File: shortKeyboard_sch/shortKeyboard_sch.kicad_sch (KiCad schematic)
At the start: 17 parts, among them J1 MPU5060 2.54 1x8, J10 In, J11 Conn_01x06, J12 Out, J2 TP4056 bat/out 2.54, J3 TP4056 in 2.54 1x6, J4 USB Power Data 2.54, J5 esp32 left 2.54 MALE, J6 esp32 right 2.54 MALE, J7 ESP32 USB 2.54 Data, J8 Li-Ion Batter 2.54, J9 Buttons Connector 2.54

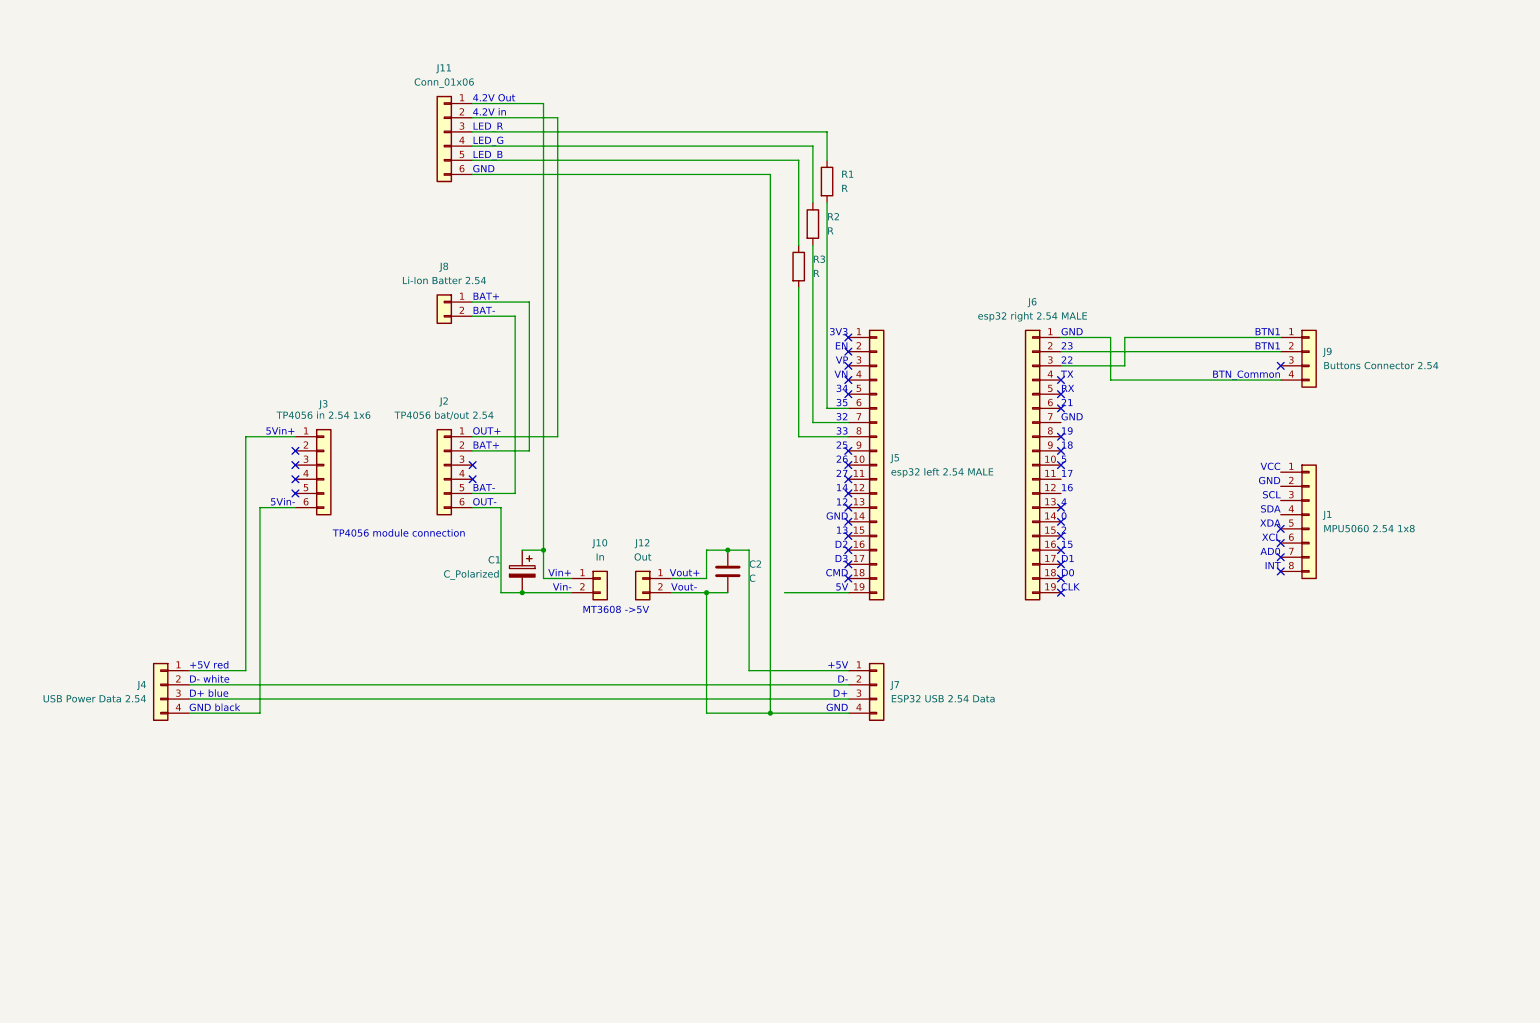
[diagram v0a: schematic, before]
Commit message: SCH change buttons connector to B1_GND_B2_GND - so buttons conectors independent
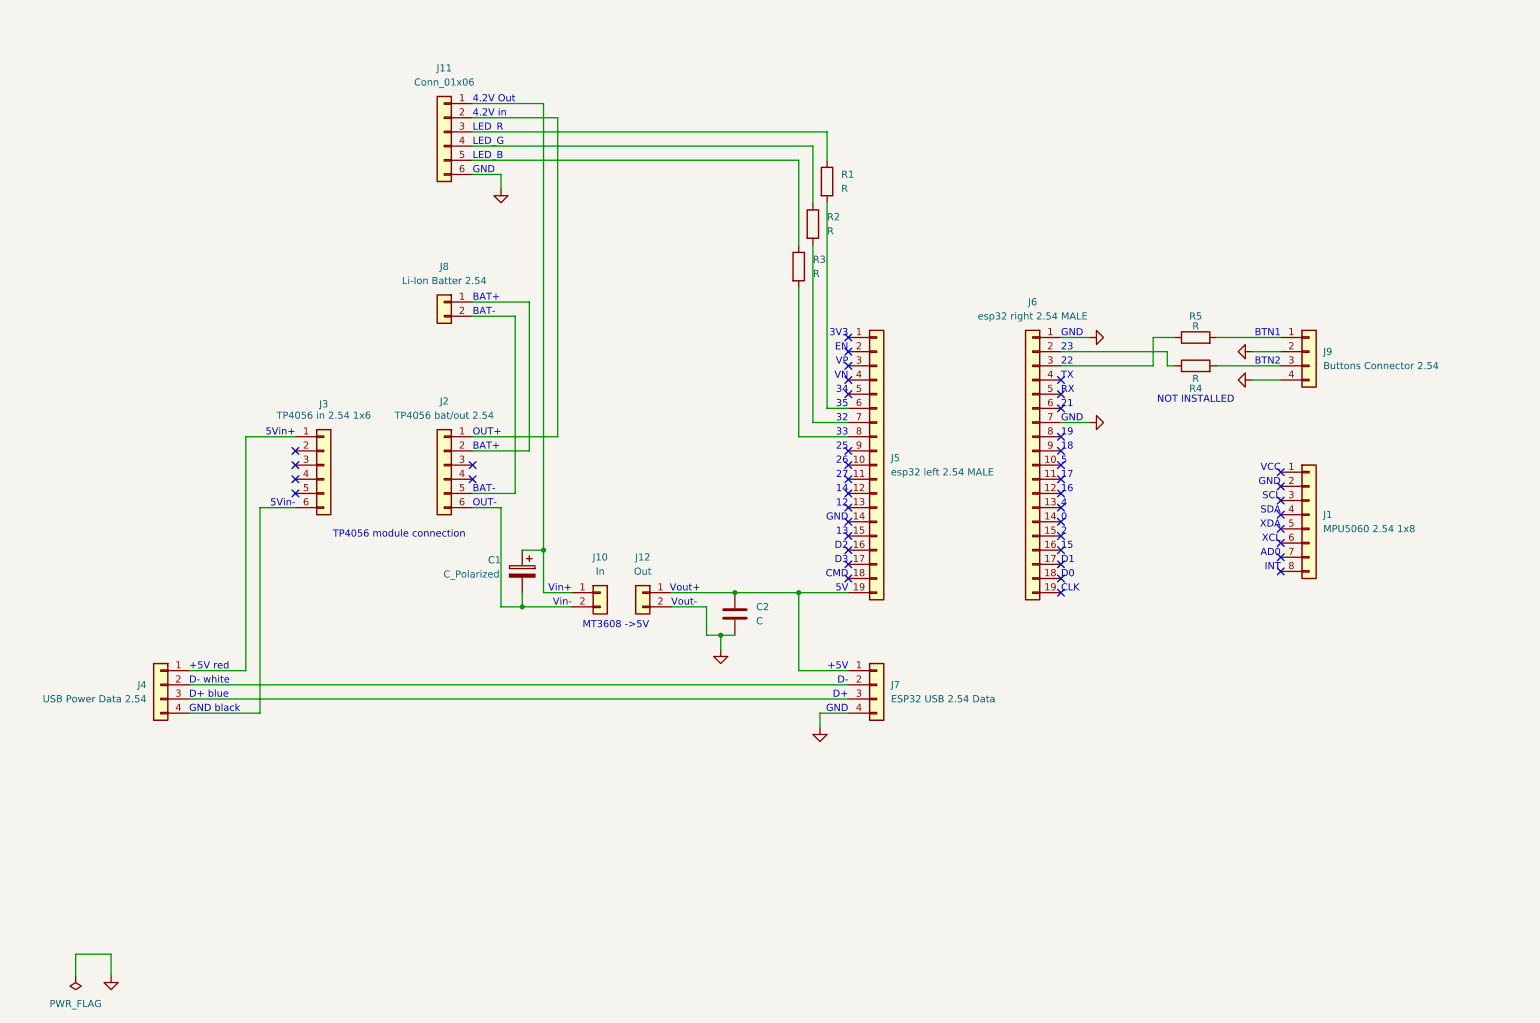
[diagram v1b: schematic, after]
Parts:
- added R4, R5: R, symbol Device:R
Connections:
- net GND: now reaches C2.2, J11.6 (Pin_6), J12.2 (Pin_2), J7.4 (Pin_4)
- net GND: now also J6.1 (Pin_1), J6.7 (Pin_7), J9.2 (Pin_2), J9.4 (Pin_4)
- net at C2.1, J12.1 (Pin_1), J7.1 (Pin_1): now also J5.19 (Pin_19)
- net at J6.2 (Pin_2): now also R4.1; no longer J9.2 (Pin_2)
- net at J6.3 (Pin_3): now also R5.1; no longer J9.1 (Pin_1)
- net at J9.3 (Pin_3): now also R4.2
- new net: J9.1 (Pin_1), R5.2
- no-connect marks 39 -> 44
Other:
- note added: "BTN2"
- note added: "NOT INSTALLED"
- note removed: "BTN_Common"
- moved on the sheet: C2, J10, J12

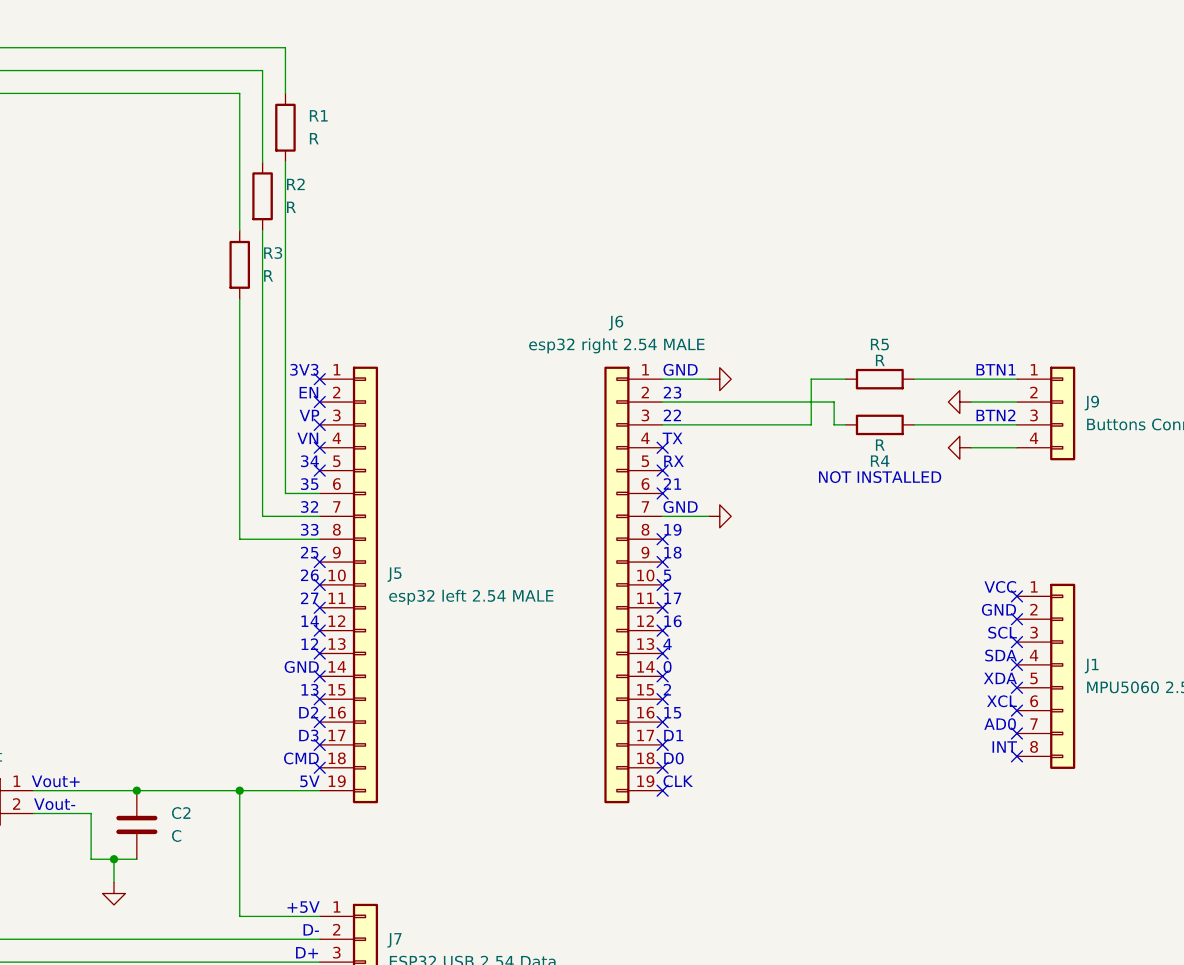
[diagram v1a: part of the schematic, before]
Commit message: update schematic, add mpu pins
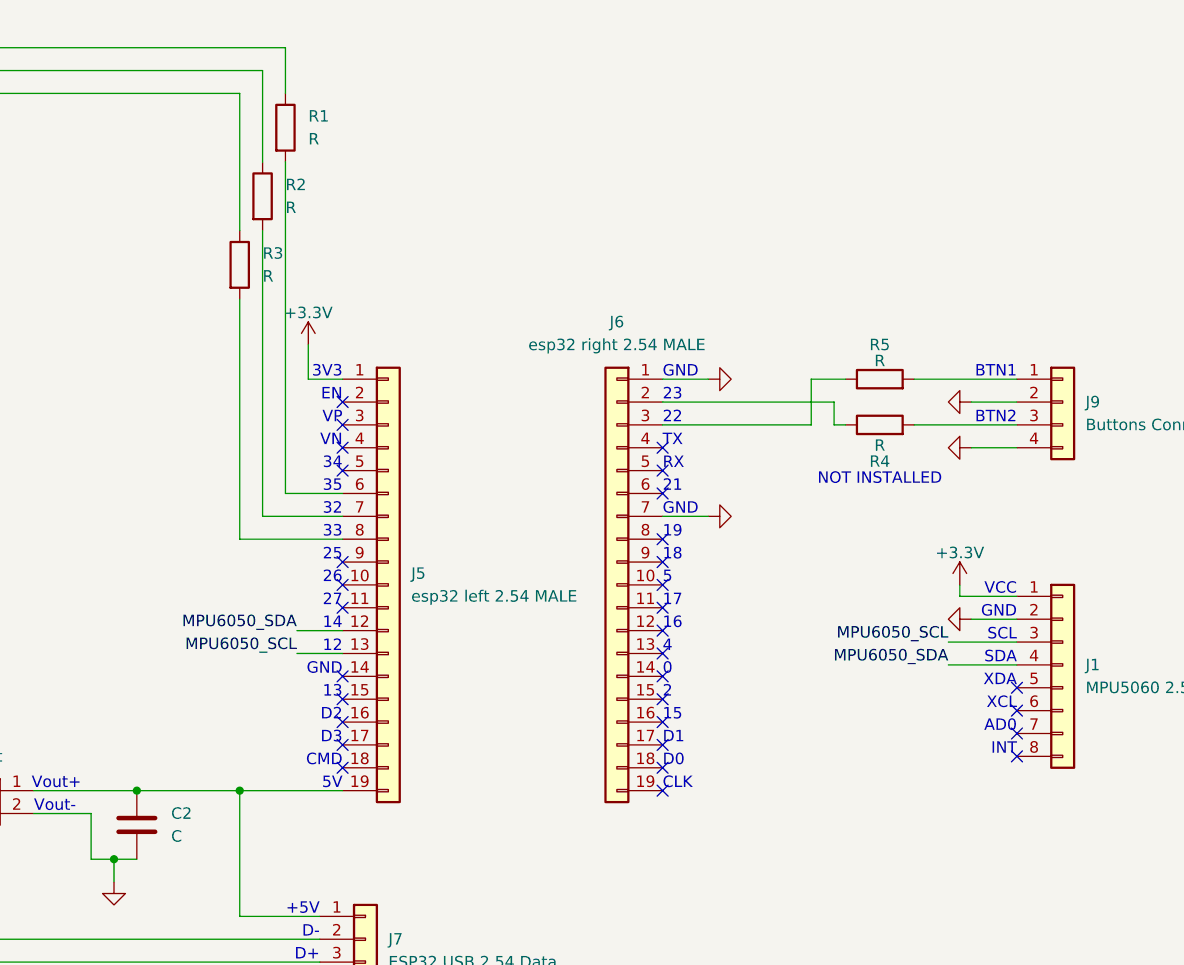
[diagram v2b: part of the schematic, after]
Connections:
- net GND: now also J1.2 (Pin_2)
- net +3.3V: now reaches J1.1 (Pin_1)
- net +3.3V: now also J5.1 (Pin_1)
- net MPU6050_SCL: now reaches J1.3 (Pin_3)
- net MPU6050_SCL: now also J5.13 (Pin_13)
- net MPU6050_SDA: now reaches J1.4 (Pin_4)
- net MPU6050_SDA: now also J5.12 (Pin_12)
- no-connect marks 44 -> 37
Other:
- moved on the sheet: J5

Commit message: intermediate new pcb version again
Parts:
- removed C1: C_Polarized, symbol Device:C_Polarized
- removed J1: MPU5060 2.54 1x8, symbol Connector_Generic:Conn_01x08
- removed J10: In, symbol Connector_Generic:Conn_01x02
- removed J11: Conn_01x06, symbol Connector_Generic:Conn_01x06
- removed J12: Out, symbol Connector_Generic:Conn_01x02
- removed J2: TP4056 bat/out 2.54, symbol Connector_Generic:Conn_01x06
- removed J3: TP4056 in 2.54 1x6, symbol Connector_Generic:Conn_01x06
- removed J4: USB Power Data 2.54, symbol Connector_Generic:Conn_01x04
- removed J5: esp32 left 2.54 MALE, symbol Connector_Generic:Conn_01x19
- removed J6: esp32 right 2.54 MALE, symbol Connector_Generic:Conn_01x19
- removed J7: ESP32 USB 2.54 Data, symbol Connector_Generic:Conn_01x04
- removed J8: Li-Ion Batter 2.54, symbol Connector_Generic:Conn_01x02
- removed J9: Buttons Connector 2.54, symbol Connector_Generic:Conn_01x04
- added C1: 22p, Capacitor_SMD:C_0805_2012Metric_Pad1.18x1.45mm_HandSolder, symbol Device:C
- added C3: 0.1u, Capacitor_SMD:C_0805_2012Metric_Pad1.18x1.45mm_HandSolder, symbol Device:C
- added C4, C5, C7: 0.1uF, Capacitor_SMD:C_0805_2012Metric_Pad1.18x1.45mm_HandSolder, symbol Device:C
- added C6: 10uF 16V, Capacitor_Tantalum_SMD:CP_EIA-3216-18_Kemet-A_HandSolder, symbol Device:C_Polarized
- added C8: 22uF 6.3V, Capacitor_Tantalum_SMD:CP_EIA-3216-18_Kemet-A_HandSolder, symbol Device:C_Polarized
- added D1, D2, D3, D5, D6: LED, LED_SMD:LED_0805_2012Metric_Pad1.15x1.40mm_HandSolder, symbol Device:LED
- added D4: SS34, Diode_SMD:D_SMA, symbol Diode:SS34
- added J1: PH2.0-4, lw_kicadLib:PH2.0-4, symbol lw_kicadLib:PH2.0-4
- added J2, J3, J6: PH2.0-2, lw_kicadLib:PH2.0-2, symbol lw_kicadLib:PH2.0-2
- added J4: WF-8, lw_kicadLib:WF-8, symbol lw_kicadLib:WF-8
- added J5: PH2.0-5, lw_kicadLib:PH2.0-5, symbol lw_kicadLib:PH2.0-5
- added Q1, Q2: SS8050, Package_TO_SOT_SMD:SOT-23, symbol Transistor_BJT:SS8050
- added Q3: AO3401A, Package_TO_SOT_SMD:SOT-23, symbol Transistor_FET:AO3401A
- added R10, R11, R6: 10к (5%), Resistor_SMD:R_0805_2012Metric_Pad1.20x1.40mm_HandSolder, symbol Device:R
- added R12, R13: 1k, Resistor_SMD:R_0805_2012Metric_Pad1.20x1.40mm_HandSolder, symbol Device:R
- added R14, R16, R18: 2.7k, Resistor_SMD:R_0805_2012Metric_Pad1.20x1.40mm_HandSolder, symbol Device:R
- added R15: 10k, Resistor_SMD:R_0805_2012Metric_Pad1.20x1.40mm_HandSolder, symbol Device:R
- added R17: 0, Resistor_SMD:R_0805_2012Metric_Pad1.20x1.40mm_HandSolder, symbol Device:R
- added U1: CH340G, Package_SO:SOIC-16_3.9x9.9mm_P1.27mm, symbol Interface_USB:CH340G
- added U2: (no value), lw_kicadLib:TP4056_Module_CD_MicroUsb, symbol lw_kicadLib:TP4056_Module
- added U3: AMS1117-3.3, Package_TO_SOT_SMD:SOT-223-3_TabPin2, symbol Regulator_Linear:AMS1117-3.3
- added U4: ESP32-WROVER, lw_kicadLib:ESP32-WROVER-handSoldering, symbol lw_kicadLib:ESP32-WROVER
- added Y1: 12M, Crystal:Crystal_SMD_HC49-SD_HandSoldering, symbol Device:Crystal
- C2: value C -> 22p; footprint (none) -> Capacitor_SMD:C_0805_2012Metric_Pad1.18x1.45mm_HandSolder
- R1, R4: value R -> ?k; footprint (none) -> Resistor_SMD:R_0805_2012Metric_Pad1.20x1.40mm_HandSolder
- R2, R3: value R -> 3.3k; footprint (none) -> Resistor_SMD:R_0805_2012Metric_Pad1.20x1.40mm_HandSolder
- R5: value R -> 10к (5%); footprint (none) -> Resistor_SMD:R_0805_2012Metric_Pad1.20x1.40mm_HandSolder
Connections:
- net GND: now also C1.2, C3.2, C4.2, C5.2, C6.2, C7.2, C8.2, J1.4 (Pin_1), J2.2 (Pin_2), J3.2 (Pin_2), J4.2 (Pin_2), J5.5 (Pin_1), R14.2, R15.2, R16.2, R18.2, U1.1 (GND), U2.2 (-5V_ext), U2.6 (-OUT), U3.1 (GND), U4.1 (GND), U4.15 (GND), U4.38 (GND), U4.39 (GND)
- net MPU6050_SCL: now also J4.3 (Pin_3), U4.14 (IO12)
- net MPU6050_SDA: now also J4.4 (Pin_4), U4.13 (IO14)
- net DTR: now reaches R4.1
- net DTR: now also R5.1, Q2.2 (E), U1.13 (~{DTR})
- net at R4.2: now also D2.1 (K)
- net at R5.2: now also Q1.1 (B)
- net RTS: now reaches R1.1
- net RTS: now also Q1.2 (E), R6.1, U1.14 (~{RTS})
- net at R2.1: now also J2.1 (Pin_1)
- net at R3.1: now also J3.1 (Pin_1)
- net at C2.1: now also U1.8 (XO), Y1.2
- net at R1.2: now also D1.1 (K)
- net BUTTON_PREV: now reaches R3.2
- net BUTTON_PREV: now also U4.36 (IO22)
- net BUTTON_NEXT: now reaches R2.2
- net BUTTON_NEXT: now also U4.37 (IO23)
- new net: R12.1, U1.2 (TXD)
- new net: R13.1, U1.3 (RXD)
- new net: J1.3 (Pin_2), U1.5 (UD+)
- new net: J1.2 (Pin_1), U1.6 (UD-)
- new net: C1.1, U1.7 (XI), Y1.1
- new net: D3.1 (K), R14.1
- new net: D5.1 (K), R16.1
- new net: Q2.1 (B), R6.2
- new net: Q3.3 (D), U2.3 (+OUT)
- new net: J6.1 (Pin_1), U2.4 (+Bat)
- new net: J6.2 (Pin_2), U2.5 (-Bat)
- new net: R17.2, U4.2 (VDD)
- new net: D6.1 (K), R18.1
- new net: D6.2 (A), U4.23 (IO15)
- new net +3V3: C3.1, C7.1, C8.1, D1.2 (A), D2.2 (A), D5.2 (A), J4.1 (Pin_1), R10.1, R11.1, R17.1, U1.16 (VCC), U1.4 (V3), U3.2 (VO)
- new net +Vin USB: D4.2 (A), J1.1 (Pin_1), Q3.1 (G), R15.1, U2.1 (+5V_ext)
- new net +Vin_AfterSW: C5.1, C6.1, D3.2 (A), J5.2 (Pin_1), U3.3 (VI)
- new net +Vin_BeforeSW: D4.1 (K), J5.1 (Pin_1), Q3.2 (S)
- new net BOOT_EN: C4.1, Q1.3 (C), R10.2, U4.3 (EN)
- new net BOOT_IO0: Q2.3 (C), R11.2, U4.25 (IO0)
- new net POWER_SW_BTN: J5.4 (Pin_1), U4.11 (IO26)
- new net POWER_SW_LED: J5.3 (Pin_2), U4.10 (IO25)
- new net UART0_RX: R12.2, U4.34 (RXD0/IO3)
- new net UART0_TX: R13.2, U4.35 (TXD0/IO1)
- no-connect marks 37 -> 31
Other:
- note added: "BAT_CHARGE"
- note added: "CH340G V3 is power out AND in(fake error)"
- note added: "CONTROLS"
- note added: "D+ Blue"
- note added: "D- White"
- note added: "DC/DC"
- note added: "For CH340C - remove oscillator"
- note added: "GND Black"
- note added: "POWER SWITCH"
- note added: "PWR_SW_BTN"
- note added: "PWR_SW_GND"
- note added: "PWR_SW_LED"
- note added: "PWR_SW_Vin"
- note added: "PWR_SW_Vout"
- note added: "UART DEBUG"
- note added: "USB->UART"
- note added: "wire colors of external USB connector"
- note removed: "+5V"
- note removed: "0"
- note removed: "12"
- note removed: "13"
- note removed: "14"
- note removed: "15"
- note removed: "16"
- note removed: "17"
- note removed: "18"
- note removed: "19"
- note removed: "2"
- note removed: "21"
- note removed: "22"
- note removed: "23"
- note removed: "25"
- note removed: "26"
- note removed: "27"
- note removed: "32"
- note removed: "33"
- note removed: "34"
- note removed: "35"
- note removed: "3V3"
- note removed: "4"
- note removed: "4.2V Out"
- note removed: "4.2V in"
- note removed: "5"
- note removed: "5V"
- note removed: "5Vin+"
- note removed: "5Vin-"
- note removed: "BTN1"
- note removed: "BTN2"
- note removed: "CLK"
- note removed: "CMD"
- note removed: "D+"
- note removed: "D+ blue"
- note removed: "D-"
- note removed: "D- white"
- note removed: "D0"
- note removed: "D1"
- note removed: "D2"
- note removed: "D3"
- note removed: "EN"
- note removed: "GND black"
- note removed: "LED_B"
- note removed: "LED_G"
- note removed: "LED_R"
- note removed: "MT3608 ->5V"
- note removed: "NOT INSTALLED"
- note removed: "OUT+"
- note removed: "OUT-"
- note removed: "RX"
- note removed: "TP4056 module connection"
- note removed: "TX"
- note removed: "VN"
- note removed: "VP"
- note removed: "Vin+"
- note removed: "Vin-"
- note removed: "Vout+"
- note removed: "Vout-"
